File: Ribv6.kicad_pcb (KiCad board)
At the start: 4 copper layers, 84.7 x 126.2 mm, 93 parts, among them J1 Conn_01x03, J10 Conn_01x19, J11 Conn_01x01_Male, J12 Conn_01x01_Male, J13 Conn_01x19, J14 Conn_02x04_Odd_Even, J15 Conn_02x04_Odd_Even, J16 Conn_01x19, J19 Conn_01x19, J2 Conn_01x02_Female, J20 Conn_01x19, J21 Conn_01x19, J22 Conn_01x06, J23 Conn_02x06_Odd_Even, J24 Conn_01x01_Male, J25 Conn_01x06, J26 Conn_01x01_Male, J3 Conn_01x19, J4 Conn_02x07_Odd_Even, J5 Conn_01x19, J6 Conn_01x02_Female, J7 Conn_01x19, J8 Conn_02x07_Odd_Even, J9 Conn_01x03, Q1 BSS138, Q10 BSS138, Q11 BSS138, Q12 BSS138, Q13 BSS138, Q14 BSS138, Q15 BSS138, Q2 BSS138, Q3 BSS138, Q4 BSS138, Q5 BSS138, Q6 BSS138, Q7 BSS138, Q8 BSS138, Q9 BSS138, U1 polulu-3784-D36V28F7, U2 polulu-3784-D36V28F7, U3 esp-devkit, U4 DPDT_x2

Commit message: finished routing.
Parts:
- moved R4 46.0 mm to (113.6, 76.5), turned to 270 degrees
- moved R5 44.0 mm to (115.1, 76.5), turned to 90 degrees
- moved Q3 40.8 mm to (117.6, 76.2), turned to 0 degrees
- moved R10 21.6 mm to (132.0, 76.7)
- moved R11 21.6 mm to (130.5, 76.7)
- moved Q5 21.6 mm to (128.0, 77.0)
- moved R2 1.08 mm to (129.5, 56.8), turned to 0 degrees
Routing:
- net SCL_33: track 115.7 -> 183.8 mm, vias 2 -> 5
- net Net-(D7-Pad1): track 0.00 -> 64.0 mm, vias 0 -> 2
- net prez: track 11.8 -> 74.3 mm, vias 1 -> 4
- net SDA_33: track 118.9 -> 178.7 mm, vias 3 -> 6
- net Net-(D6-Pad1): track 0.00 -> 57.3 mm, vias 0 -> 2
- net Net-(D4-Pad1): track 5.71 -> 57.1 mm, vias 0 -> 2
- net +3V3: track 252.1 -> 298.2 mm, vias 11 -> 12
- net Net-(D3-Pad1): track 0.00 -> 40.0 mm, vias 0 -> 2
- net Net-(D5-Pad1): track 52.7 -> 68.1 mm
- net GND: track 61.8 -> 76.0 mm, vias 4 -> 6
- net +5V: track 291.6 -> 300.8 mm
- net +BATT: track 104.3 -> 100.6 mm
- net UBEC1: track 9.53 -> 13.1 mm
- net Net-(Q2-Pad1): track 0.00 -> 3.24 mm
- net Net-(Q6-Pad1): track 0.00 -> 3.24 mm
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
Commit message: Added LED on pin 13
#6
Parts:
- added D8: LED_Small, LED_SMD:LED_0805_2012Metric, F.Cu at (112.8, 158.0)
- added R39: 330, Resistor_SMD:R_0603_1608Metric, F.Cu at (112.8, 154.5)
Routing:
- net Net-(J13-Pad15): track 10.2 -> 39.7 mm, vias 0 -> 1
- net GND: track 76.0 -> 78.3 mm, vias 6 -> 7
- net Net-(D8-Pad2): track 0.00 -> 1.78 mm
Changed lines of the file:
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@@
     (thickness 1.6)
     (drawings 100)
-    (tracks 865)
+    (tracks 877)
     (zones 0)
-    (modules 93)
-    (nets 98)
+    (modules 95)
+    (nets 99)
   )
   (page A4)
@@
   (net 96 "Net-(Q1-Pad1)")
   (net 97 "Net-(Q7-Pad1)")
+  (net 98 "Net-(D8-Pad2)")
   (net_class Default "This is the default net class."
     (clearance 0.2)
@@
     (add_net "Net-(D7-Pad1)")
     (add_net "Net-(D7-Pad2)")
+    (add_net "Net-(D8-Pad2)")
     (add_net "Net-(F1-Pad1)")
     (add_net "Net-(F2-Pad1)")
@@
     )
   )
+  (module LED_SMD:LED_0805_2012Metric (layer F.Cu)
+    (at 112.75 158 90)
+    (descr "LED SMD 0805 (2012 Metric), square (rectangular) end terminal, IPC_7351 nominal, (Body size source: https://docs.google.com/spreadsheets/d/1BsfQQcO9C6DZCsRaXUlFlo91Tg2WpOkGARC1WS5S8t0/edit?usp=sharing), generated with kicad-footprint-generator")
+    (tags diode)
+    (attr smd)
+    (fp_text reference D8 (at 0 -1.65 90) (layer F.SilkS)
+      (effects (font (size 1 1) (thickness 0.15)))
+    )
+    (fp_text value LED_Small (at 0 1.65 90) (layer F.Fab)
+      (effects (font (size 1 1) (thickness 0.15)))
+    )
+    (fp_line (start 1 -0.6) (end -0.7 -0.6) (layer F.Fab) (width 0.1))
+    (fp_line (start -0.7 -0.6) (end -1 -0.3) (layer F.Fab) (width 0.1))
+    (fp_line (start -1 -0.3) (end -1 0.6) (layer F.Fab) (width 0.1))
+    (fp_line (start -1 0.6) (end 1 0.6) (layer F.Fab) (width 0.1))
+    (fp_line (start 1 0.6) (end 1 -0.6) (layer F.Fab) (width 0.1))
+    (fp_line (start 1 -0.96) (end -1.685 -0.96) (layer F.SilkS) (width 0.12))
+    (fp_line (start -1.685 -0.96) (end -1.685 0.96) (layer F.SilkS) (width 0.12))
+    (fp_line (start -1.685 0.96) (end 1 0.96) (layer F.SilkS) (width 0.12))
+    (fp_line (start -1.68 0.95) (end -1.68 -0.95) (layer F.CrtYd) (width 0.05))
+    (fp_line (start -1.68 -0.95) (end 1.68 -0.95) (layer F.CrtYd) (width 0.05))
+    (fp_line (start 1.68 -0.95) (end 1.68 0.95) (layer F.CrtYd) (width 0.05))
+    (fp_line (start 1.68 0.95) (end -1.68 0.95) (layer F.CrtYd) (width 0.05))
+    (fp_text user %R (at 0 0 90) (layer F.Fab)
+      (effects (font (size 0.5 0.5) (thickness 0.08)))
+    )
+    (pad 1 smd roundrect (at -0.9375 0 90) (size 0.975 1.4) (layers F.Cu F.Paste F.Mask) (roundrect_rratio 0.25)
+      (net 1 GND))
+    (pad 2 smd roundrect (at 0.9375 0 90) (size 0.975 1.4) (layers F.Cu F.Paste F.Mask) (roundrect_rratio 0.25)
+      (net 98 "Net-(D8-Pad2)"))
+    (model ${KISYS3DMOD}/LED_SMD.3dshapes/LED_0805_2012Metric.wrl
+      (at (xyz 0 0 0))
+      (scale (xyz 1 1 1))
+      (rotate (xyz 0 0 0))
+    )
+  )
+  (module Resistor_SMD:R_0603_1608Metric (layer F.Cu)
+    (at 112.75 154.5 90)
+    (descr "Resistor SMD 0603 (1608 Metric), square (rectangular) end terminal, IPC_7351 nominal, (Body size source: http://www.tortai-tech.com/upload/download/2011102023233369053.pdf), generated with kicad-footprint-generator")
+    (tags resistor)
+    (attr smd)
+    (fp_text reference R39 (at 0 -1.43 90) (layer F.SilkS)
+      (effects (font (size 1 1) (thickness 0.15)))
+    )
+    (fp_text value 330 (at 0 1.43 90) (layer F.Fab)
+      (effects (font (size 1 1) (thickness 0.15)))
+    )
+    (fp_line (start -0.8 0.4) (end -0.8 -0.4) (layer F.Fab) (width 0.1))
+    (fp_line (start -0.8 -0.4) (end 0.8 -0.4) (layer F.Fab) (width 0.1))
+    (fp_line (start 0.8 -0.4) (end 0.8 0.4) (layer F.Fab) (width 0.1))
+    (fp_line (start 0.8 0.4) (end -0.8 0.4) (layer F.Fab) (width 0.1))
+    (fp_line (start -0.162779 -0.51) (end 0.162779 -0.51) (layer F.SilkS) (width 0.12))
+    (fp_line (start -0.162779 0.51) (end 0.162779 0.51) (layer F.SilkS) (width 0.12))
+    (fp_line (start -1.48 0.73) (end -1.48 -0.73) (layer F.CrtYd) (width 0.05))
+    (fp_line (start -1.48 -0.73) (end 1.48 -0.73) (layer F.CrtYd) (width 0.05))
+    (fp_line (start 1.48 -0.73) (end 1.48 0.73) (layer F.CrtYd) (width 0.05))
+    (fp_line (start 1.48 0.73) (end -1.48 0.73) (layer F.CrtYd) (width 0.05))
+    (fp_text user %R (at 0 0 90) (layer F.Fab)
+      (effects (font (size 0.4 0.4) (thickness 0.06)))
+    )
+    (pad 1 smd roundrect (at -0.7875 0 90) (size 0.875 0.95) (layers F.Cu F.Paste F.Mask) (roundrect_rratio 0.25)
+      (net 98 "Net-(D8-Pad2)"))
+    (pad 2 smd roundrect (at 0.7875 0 90) (size 0.875 0.95) (layers F.Cu F.Paste F.Mask) (roundrect_rratio 0.25)
+      (net 31 "Net-(J13-Pad15)"))
+    (model ${KISYS3DMOD}/Resistor_SMD.3dshapes/R_0603_1608Metric.wrl
+      (at (xyz 0 0 0))
+      (scale (xyz 1 1 1))
+      (rotate (xyz 0 0 0))
+    )
+  )
   (gr_line (start 167.8421 34.6441) (end 167.8421 39.6441) (layer Edge.Cuts) (width 0.1))
   (gr_line (start 83.0961 34.6441) (end 83.0961 44.6405) (layer Edge.Cuts) (width 0.1))
@@
   (segment (start 88.45 90.0125) (end 88.45 90.25) (width 0.25) (layer F.Cu) (net 1))
   (segment (start 90.25 88.2125) (end 88.45 90.0125) (width 0.25) (layer F.Cu) (net 1))
+  (via (at 115 159) (size 0.8) (drill 0.4) (layers F.Cu B.Cu) (net 1))
+  (segment (start 112.75 158.9375) (end 114.9375 158.9375) (width 0.25) (layer F.Cu) (net 1))
+  (segment (start 114.9375 158.9375) (end 115 159) (width 0.25) (layer F.Cu) (net 1))
   (segment (start 162.5625 94.15) (end 162.4625 94.25) (width 0.25) (layer F.Cu) (net 2))
   (segment (start 162.5625 92.25) (end 162.5625 94.15) (width 0.25) (layer F.Cu) (net 2))
@@
   (segment (start 102.7303 131.8641) (end 107.8103 131.8641) (width 0.25) (layer F.Cu) (net 31))
   (segment (start 107.8103 131.8641) (end 112.8961 131.8641) (width 0.25) (layer F.Cu) (net 31))
+  (segment (start 113.211612 153.250888) (end 113.211612 150.038388) (width 0.25) (layer F.Cu) (net 31))
+  (segment (start 112.75 153.7125) (end 113.211612 153.250888) (width 0.25) (layer F.Cu) (net 31))
+  (via (at 119.263973 143.513973) (size 0.8) (drill 0.4) (layers F.Cu B.Cu) (net 31))
+  (segment (start 113.211612 150.038388) (end 119.263973 143.986027) (width 0.25) (layer F.Cu) (net 31))
+  (segment (start 119.263973 143.986027) (end 119.263973 143.513973) (width 0.25) (layer F.Cu) (net 31))
+  (segment (start 119.263973 143.513973) (end 119.263973 134.263973) (width 0.25) (layer B.Cu) (net 31))
+  (segment (start 116.8641 131.8641) (end 112.8961 131.8641) (width 0.25) (layer B.Cu) (net 31))
+  (segment (start 119.263973 134.263973) (end 116.8641 131.8641) (width 0.25) (layer B.Cu) (net 31))
   (segment (start 112.8961 134.4041) (end 107.8103 134.4041) (width 0.25) (layer F.Cu) (net 32))
   (segment (start 107.8103 134.4041) (end 102.7303 134.4041) (width 0.25) (layer F.Cu) (net 32))
@@
   (segment (start 86.55 90.25) (end 86.55 90.3) (width 0.25) (layer F.Cu) (net 97))
   (segment (start 86.55 90.3) (end 87.7125 91.4625) (width 0.25) (layer F.Cu) (net 97))
+  (segment (start 112.75 157.0625) (end 112.75 155.2875) (width 0.25) (layer F.Cu) (net 98))
   (zone (net 1) (net_name GND) (layer B.Cu) (hatch edge 0.508)
     (connect_pads (clearance 0.508))

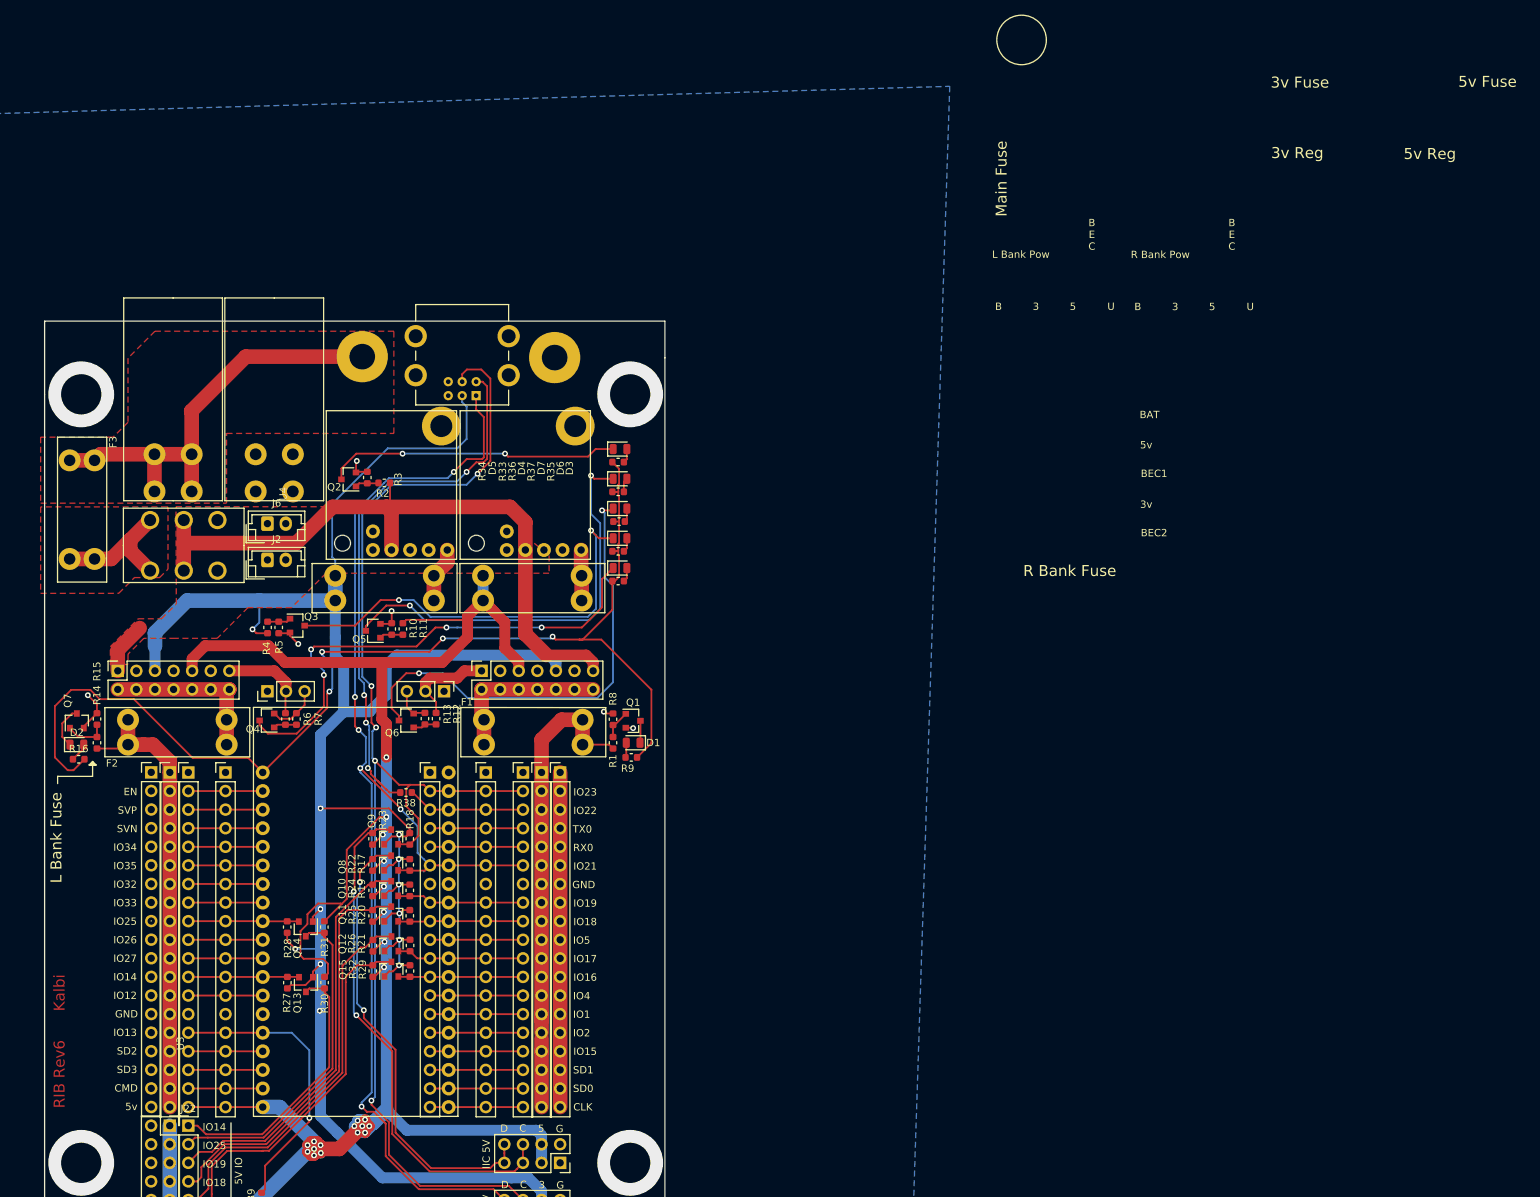
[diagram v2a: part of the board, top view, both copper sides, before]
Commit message: Board Updates.
#3 Updated power system for the rib
 * Bolt holes on a 5.5mm grid
 * Second ehader added so narrow ESP32 devkit can be used
 * Accepts a 7.5 to 18v battery with solder lugs and bannana plugs
 * 5v 2 amp REG for esp32
 * 2 external power converter ports
 * Both banks are switchable via jumpers between sys5, raw, ext reg, sensor 3v3
 * GPIO 0  connects to io
 * RST connects to IO
 * 5v shifter on i2c and 5v i2c on a header.
 * shifted bidirectional 3 to 5 level shifters for pins 19,18,17,16,25,14
 * Updated Silkscreen

#5 Added a switch
#6 LED on pin 13
#9 #10 changed Circuit. LEDs light up when power is applied
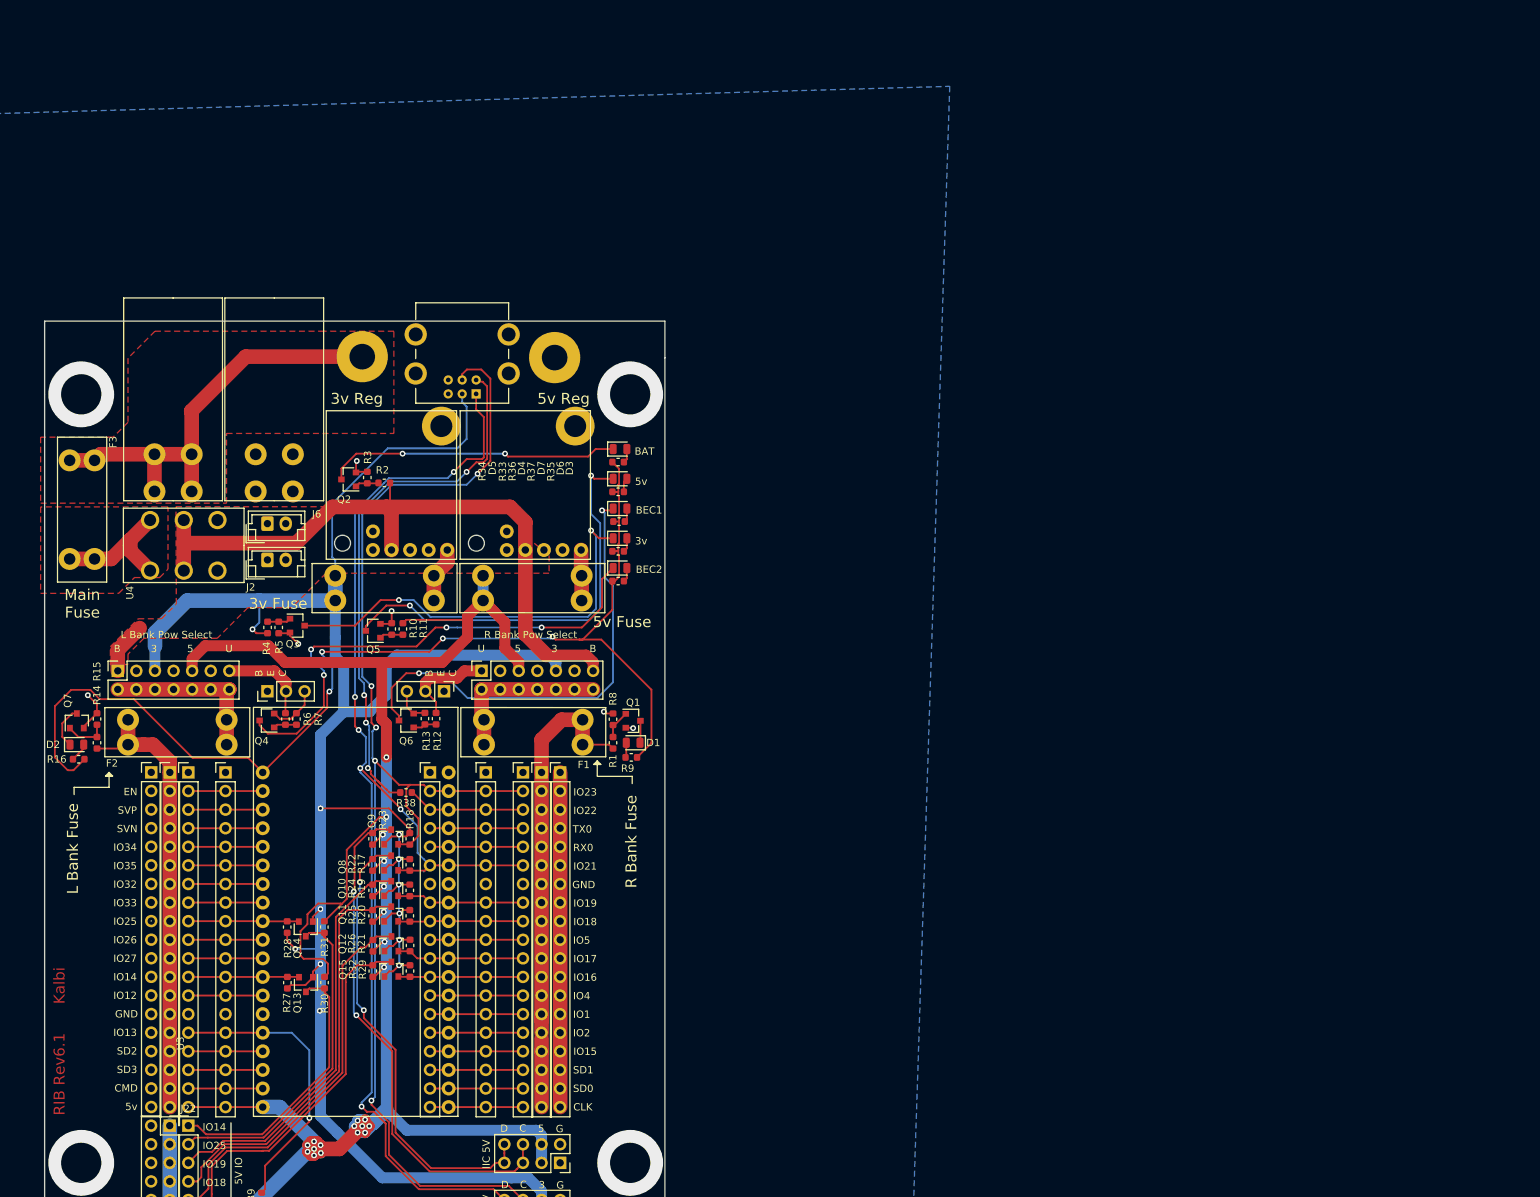
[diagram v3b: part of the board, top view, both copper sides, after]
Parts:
- moved J25 0.24 mm to (140.1, 39.0)
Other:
- board text added: "L Bank Pow Select"
- board text added: "R Bank Pow Select"
- board text added: "RIB Rev6.1 Kalbi"
- board text removed: "L Bank Pow"
- board text removed: "R Bank Pow"
- board text removed: "RIB Rev6 Kalbi"

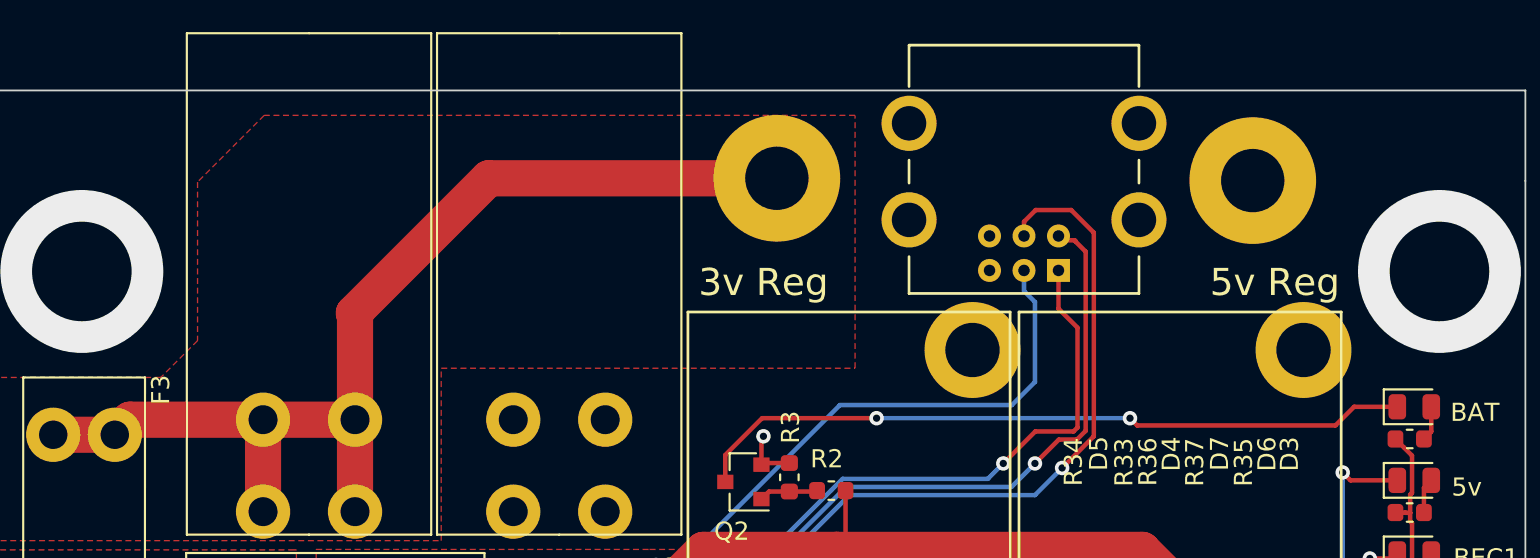
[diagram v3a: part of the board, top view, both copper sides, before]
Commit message: Added labels to power lugs, Bannana jacks #12
Added labels to power lugs, Bannana jacks #12
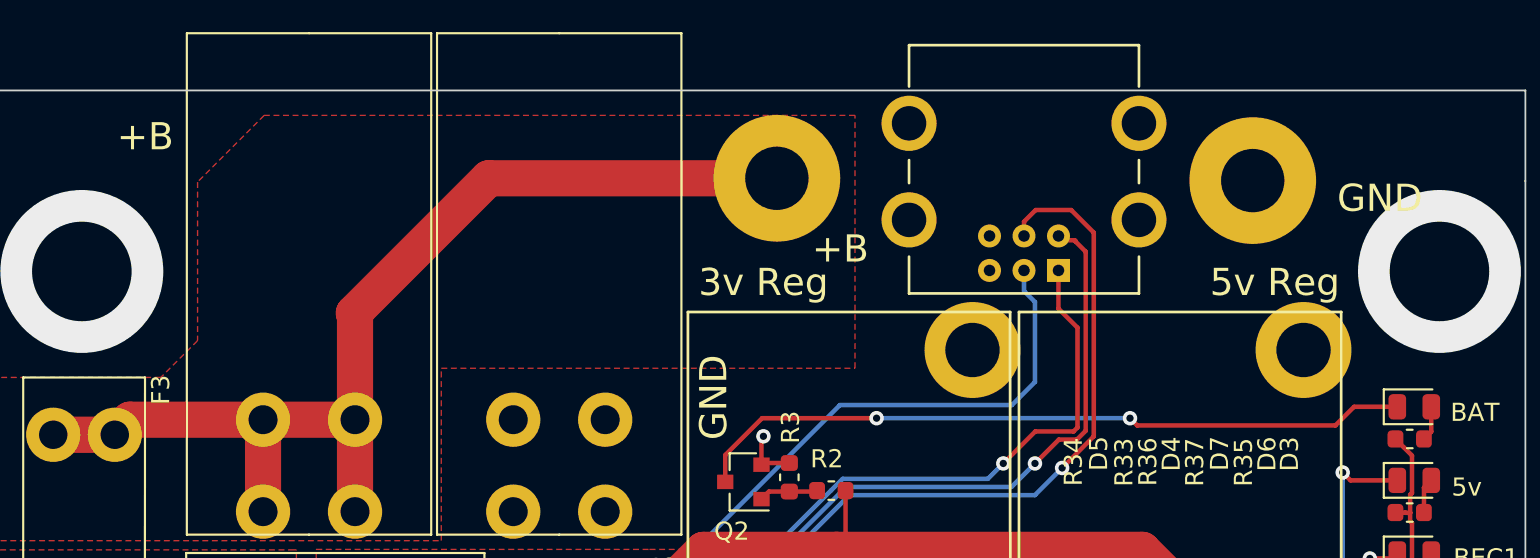
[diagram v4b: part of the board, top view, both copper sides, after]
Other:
- board text added: "+B"
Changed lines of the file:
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@@
   (general
     (thickness 1.6)
-    (drawings 110)
+    (drawings 114)
     (tracks 877)
     (zones 0)
@@
     )
   )
+  (gr_text GND (at 123 51.6 90) (layer F.SilkS)
+    (effects (font (size 1.5 1.5) (thickness 0.3)))
+  )
+  (gr_text +B (at 91.6 37.2) (layer F.SilkS)
+    (effects (font (size 1.5 1.5) (thickness 0.3)))
+  )
+  (gr_text GND (at 159.8 40.6) (layer F.SilkS)
+    (effects (font (size 1.5 1.5) (thickness 0.3)))
+  )
+  (gr_text +B (at 130 43.4) (layer F.SilkS)
+    (effects (font (size 1.5 1.5) (thickness 0.3)))
+  )
   (gr_text "L Bank Pow Select" (at 99.75 77.5) (layer F.SilkS)
